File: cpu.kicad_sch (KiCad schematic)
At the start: 17 parts, among them IC1 68000CC

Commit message: Start PCB layout.
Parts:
- C15, C16, C17, C18, C2, C3, C5: footprint (none) -> Capacitor_SMD:C_0805_2012Metric
- IC1: value 68000CC -> 68HC000; footprint (none) -> Package_LCC:PLCC-68
- IC2: footprint (none) -> Package_SO:VSO-40_7.6x15.4mm_P0.762mm
- IC7: renamed from IC3; footprint (none) -> Package_SO:VSO-40_7.6x15.4mm_P0.762mm
- R3: footprint (none) -> Resistor_SMD:R_0805_2012Metric
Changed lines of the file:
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@@
       (effects (font (size 1.27 1.27)) (justify left))
     )
-    (property "Value" "68000CC" (at 171.1041 55.88 0)
-      (effects (font (size 1.27 1.27)) (justify left))
-    )
-    (property "Footprint" "" (at 166.37 115.57 0)
+    (property "Value" "68HC000" (at 171.1041 55.88 0)
+      (effects (font (size 1.27 1.27)) (justify left))
+    )
+    (property "Footprint" "Package_LCC:PLCC-68" (at 166.37 115.57 0)
       (effects (font (size 1.27 1.27)) hide)
     )
@@
       (effects (font (size 1.27 1.27)) (justify left))
     )
-    (property "Footprint" "" (at 66.3702 234.95 0)
+    (property "Footprint" "Capacitor_SMD:C_0805_2012Metric" (at 66.3702 234.95 0)
       (effects (font (size 1.27 1.27)) hide)
     )
@@
   (symbol (lib_id "MegaDrive:VRAM_64Kx8") (at 301.625 193.675 0) (unit 1)
     (in_bom yes) (on_board yes) (dnp no) (fields_autoplaced)
-    (property "Reference" "IC3" (at 305.0891 167.64 0)
+    (property "Reference" "IC7" (at 305.0891 167.64 0)
       (effects (font (size 1.27 1.27)) (justify left))
     )
@@
       (effects (font (size 1.27 1.27)))
     )
-    (property "Footprint" "" (at 302.26 196.85 0)
+    (property "Footprint" "Package_SO:VSO-40_7.6x15.4mm_P0.762mm" (at 302.26 196.85 0)
       (effects (font (size 1.27 1.27)) hide)
     )
@@
       (project "Neptune"
         (path "/bcc23b51-b742-4ae5-9dd6-d96a24058944/48e60f61-77cc-4ea0-898f-0029aa970ca5"
-          (reference "IC3") (unit 1)
+          (reference "IC7") (unit 1)
         )
       )
@@
       (effects (font (size 1.27 1.27)) (justify left))
     )
-    (property "Footprint" "" (at 350.8502 220.345 0)
+    (property "Footprint" "Capacitor_SMD:C_0805_2012Metric" (at 350.8502 220.345 0)
       (effects (font (size 1.27 1.27)) hide)
     )
@@
       (effects (font (size 1.27 1.27)) (justify right))
     )
-    (property "Footprint" "" (at 196.85 165.608 90)
+    (property "Footprint" "Resistor_SMD:R_0805_2012Metric" (at 196.85 165.608 90)
       (effects (font (size 1.27 1.27)) hide)
     )
@@
       (effects (font (size 1.27 1.27)) (justify left))
     )
-    (property "Footprint" "" (at 332.4098 220.345 0)
+    (property "Footprint" "Capacitor_SMD:C_0805_2012Metric" (at 332.4098 220.345 0)
       (effects (font (size 1.27 1.27)) hide)
     )
@@
       (effects (font (size 1.27 1.27)) (justify right))
     )
-    (property "Footprint" "" (at 135.255 137.668 90)
+    (property "Footprint" "Resistor_SMD:R_0805_2012Metric" (at 135.255 137.668 90)
       (effects (font (size 1.27 1.27)) hide)
     )
@@
       (effects (font (size 1.27 1.27)) (justify left))
     )
-    (property "Footprint" "" (at 359.1052 220.345 0)
+    (property "Footprint" "Capacitor_SMD:C_0805_2012Metric" (at 359.1052 220.345 0)
       (effects (font (size 1.27 1.27)) hide)
     )
@@
       (effects (font (size 1.27 1.27)) (justify left))
     )
-    (property "Footprint" "" (at 342.5952 220.345 0)
+    (property "Footprint" "Capacitor_SMD:C_0805_2012Metric" (at 342.5952 220.345 0)
       (effects (font (size 1.27 1.27)) hide)
     )
@@
       (effects (font (size 1.27 1.27)) (justify left))
     )
-    (property "Footprint" "" (at 272.1102 115.57 0)
+    (property "Footprint" "Capacitor_SMD:C_0805_2012Metric" (at 272.1102 115.57 0)
       (effects (font (size 1.27 1.27)) hide)
     )
@@
       (effects (font (size 1.27 1.27)) (justify left))
     )
-    (property "Footprint" "" (at 286.0802 115.57 0)
+    (property "Footprint" "Capacitor_SMD:C_0805_2012Metric" (at 286.0802 115.57 0)
       (effects (font (size 1.27 1.27)) hide)
     )
@@
       (effects (font (size 1.27 1.27)))
     )
-    (property "Footprint" "" (at 249.555 76.835 0)
+    (property "Footprint" "Package_SO:VSO-40_7.6x15.4mm_P0.762mm" (at 249.555 76.835 0)
       (effects (font (size 1.27 1.27)) hide)
     )
@@
         )
         (path "/bcc23b51-b742-4ae5-9dd6-d96a24058944/48e60f61-77cc-4ea0-898f-0029aa970ca5"
-          (reference "FB1") (unit 1)
-        )
-      )
+          (reference "FB7") (unit 1)
+        )
+      )

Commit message: Save first mock-up before updating footprints.
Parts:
- CA1, CA2, CA3, CA4: footprint (none) -> Resistor_SMD:R_Array_Convex_4x0603
- FB7: footprint (none) -> Inductor_SMD:L_0805_2012Metric
- IC2: footprint Package_SO:VSO-40_7.6x15.4mm_P0.762mm -> Neptune:SOIC-40
- IC7: footprint Package_SO:VSO-40_7.6x15.4mm_P0.762mm -> Neptune:SOJ-40
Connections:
- net SC renamed ~{SC}
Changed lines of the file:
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@@
     )
   )
-  (global_label "SC" (shape input) (at 365.76 209.55 0) (fields_autoplaced)
+  (global_label "~{SC}" (shape input) (at 365.76 209.55 0) (fields_autoplaced)
     (effects (font (size 1.27 1.27)) (justify left))
     (property "Intersheetrefs" "${INTERSHEET_REFS}" (at 371.2247 209.55 0)
@@
       (effects (font (size 1.27 1.27)) (justify left))
     )
-    (property "Footprint" "" (at 150.495 231.14 90)
+    (property "Footprint" "Resistor_SMD:R_Array_Convex_4x0603" (at 150.495 231.14 90)
       (effects (font (size 1.27 1.27)) hide)
     )
@@
       (effects (font (size 1.27 1.27)))
     )
-    (property "Footprint" "Package_SO:VSO-40_7.6x15.4mm_P0.762mm" (at 302.26 196.85 0)
+    (property "Footprint" "Neptune:SOJ-40" (at 302.26 196.85 0)
       (effects (font (size 1.27 1.27)) hide)
     )
@@
       (effects (font (size 1.27 1.27)) (justify left))
     )
-    (property "Footprint" "" (at 109.855 231.14 90)
+    (property "Footprint" "Resistor_SMD:R_Array_Convex_4x0603" (at 109.855 231.14 90)
       (effects (font (size 1.27 1.27)) hide)
     )
@@
       (effects (font (size 1.27 1.27)) (justify left))
     )
-    (property "Footprint" "" (at 130.175 231.14 90)
+    (property "Footprint" "Resistor_SMD:R_Array_Convex_4x0603" (at 130.175 231.14 90)
       (effects (font (size 1.27 1.27)) hide)
     )
@@
       (effects (font (size 1.27 1.27)) (justify left))
     )
-    (property "Footprint" "" (at 170.18 231.14 90)
+    (property "Footprint" "Resistor_SMD:R_Array_Convex_4x0603" (at 170.18 231.14 90)
       (effects (font (size 1.27 1.27)) hide)
     )
@@
       (effects (font (size 1.27 1.27)))
     )
-    (property "Footprint" "Package_SO:VSO-40_7.6x15.4mm_P0.762mm" (at 249.555 76.835 0)
+    (property "Footprint" "Neptune:SOIC-40" (at 249.555 76.835 0)
       (effects (font (size 1.27 1.27)) hide)
     )
@@
       (effects (font (size 1.27 1.27)))
     )
-    (property "Footprint" "" (at 135.255 61.468 90)
-      (effects (font (size 1.27 1.27)) hide)
-    )
+    (property "Footprint" "Inductor_SMD:L_0805_2012Metric" (at 135.255 61.468 90)
+      (effects (font (size 1.27 1.27)) hide)
+    )

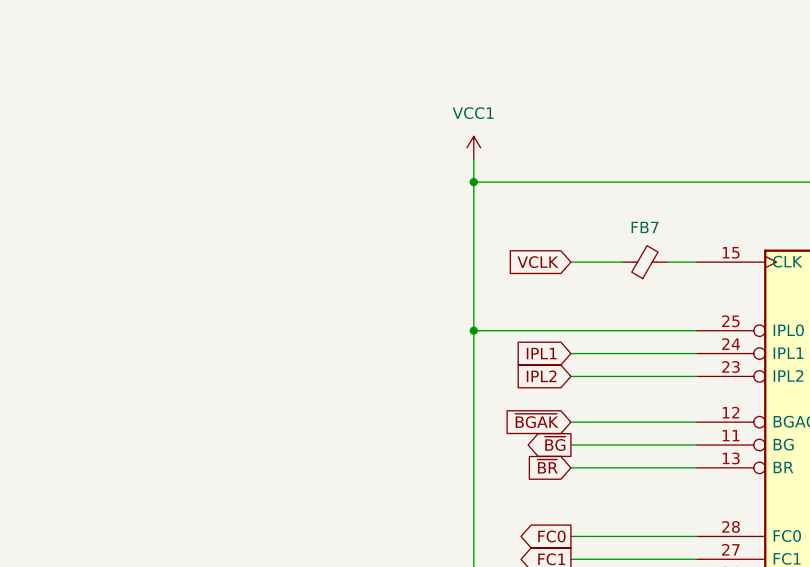
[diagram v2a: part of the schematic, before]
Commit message: Draft new layout with more accurate footprints.
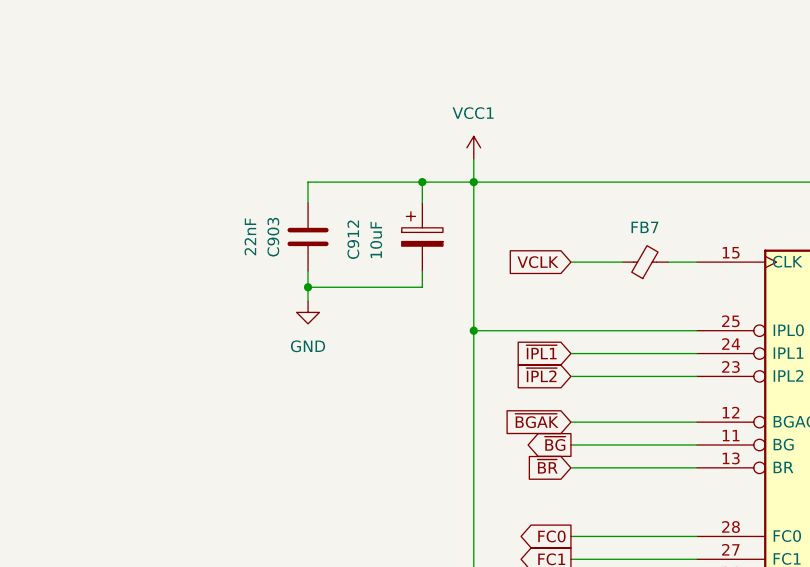
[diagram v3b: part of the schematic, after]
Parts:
- added C903: 22nF, Capacitor_SMD:C_0805_2012Metric, symbol Device:C
- added C912: 10uF, Capacitor_THT:CP_Radial_D5.0mm_P2.50mm, symbol Device:C_Polarized
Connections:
- net GND: now also C903.1, C912.2
- net VCC1: now also C903.2, C912.1
- net IPL1 renamed ~{IPL1}
- net IPL2 renamed ~{IPL2}
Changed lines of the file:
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@@
   (junction (at 118.11 241.3) (diameter 0) (color 0 0 0 0)
   )
+  (junction (at 97.79 62.484) (diameter 0) (color 0 0 0 0)
+  )
   (junction (at 158.115 241.3) (diameter 0) (color 0 0 0 0)
   )
@@
   )
   (junction (at 333.375 209.55) (diameter 0) (color 0 0 0 0)
+  )
+  (junction (at 110.49 50.8) (diameter 0) (color 0 0 0 0)
   )
   (junction (at 285.115 117.475) (diameter 0) (color 0 0 0 0)
@@
     (stroke (width 0) (type default))
   )
+  (wire (pts (xy 97.79 50.8) (xy 110.49 50.8))
+    (stroke (width 0) (type default))
+  )
   (bus (pts (xy 272.415 211.455) (xy 272.415 208.915))
     (stroke (width 0) (type default))
@@
     (stroke (width 0) (type default))
   )
+  (wire (pts (xy 97.79 53.086) (xy 97.79 50.8))
+    (stroke (width 0) (type default))
+  )
   (wire (pts (xy 349.885 220.345) (xy 349.885 222.885))
     (stroke (width 0) (type default))
@@
     (stroke (width 0) (type default))
   )
+  (wire (pts (xy 116.205 50.8) (xy 166.37 50.8))
+    (stroke (width 0) (type default))
+  )
   (bus (pts (xy 220.98 90.17) (xy 220.98 87.63))
     (stroke (width 0) (type default))
@@
     (stroke (width 0) (type default))
   )
+  (wire (pts (xy 110.49 50.8) (xy 116.205 50.8))
+    (stroke (width 0) (type default))
+  )
+  (wire (pts (xy 97.79 62.484) (xy 97.79 64.008))
+    (stroke (width 0) (type default))
+  )
   (wire (pts (xy 266.065 105.41) (xy 285.115 105.41))
     (stroke (width 0) (type default))
@@
     (stroke (width 0) (type default))
   )
+  (wire (pts (xy 110.49 62.484) (xy 97.79 62.484))
+    (stroke (width 0) (type default))
+  )
   (wire (pts (xy 285.115 117.475) (xy 271.145 117.475))
     (stroke (width 0) (type default))
@@
     (stroke (width 0) (type default))
   )
+  (wire (pts (xy 110.49 50.8) (xy 110.49 53.086))
+    (stroke (width 0) (type default))
+  )
   (wire (pts (xy 341.63 196.85) (xy 365.76 196.85))
     (stroke (width 0) (type default))
@@
     (stroke (width 0) (type default))
   )
+  (wire (pts (xy 97.79 60.706) (xy 97.79 62.484))
+    (stroke (width 0) (type default))
+  )
   (bus (pts (xy 277.495 92.71) (xy 277.495 90.17))
     (stroke (width 0) (type default))
@@
     (stroke (width 0) (type default))
   )
+  (wire (pts (xy 110.49 60.706) (xy 110.49 62.484))
+    (stroke (width 0) (type default))
+  )
   (bus (pts (xy 272.415 167.64) (xy 272.415 170.815))
     (stroke (width 0) (type default))
@@
   )
   (wire (pts (xy 191.77 110.49) (xy 200.66 110.49))
-    (stroke (width 0) (type default))
-  )
-  (wire (pts (xy 116.205 50.8) (xy 166.37 50.8))
     (stroke (width 0) (type default))
   )
@@
     )
   )
-  (global_label "IPL2" (shape input) (at 127 72.39 180) (fields_autoplaced)
+  (global_label "~{IPL2}" (shape input) (at 127 72.39 180) (fields_autoplaced)
     (effects (font (size 1.27 1.27)) (justify right))
     (property "Intersheetrefs" "${INTERSHEET_REFS}" (at 119.9024 72.39 0)
@@
     )
   )
-  (global_label "IPL1" (shape input) (at 127 69.85 180) (fields_autoplaced)
+  (global_label "~{IPL1}" (shape input) (at 127 69.85 180) (fields_autoplaced)
     (effects (font (size 1.27 1.27)) (justify right))
     (property "Intersheetrefs" "${INTERSHEET_REFS}" (at 119.9024 69.85 0)
@@
     )
   )
+  (symbol (lib_id "power:GND") (at 97.79 64.008 0) (mirror y) (unit 1)
+    (in_bom yes) (on_board yes) (dnp no) (fields_autoplaced)
+    (property "Reference" "#PWR010" (at 97.79 70.358 0)
+      (effects (font (size 1.27 1.27)) hide)
+    )
+    (property "Value" "GND" (at 97.79 69.088 0)
+      (effects (font (size 1.27 1.27)))
+    )
+    (property "Footprint" "" (at 97.79 64.008 0)
+      (effects (font (size 1.27 1.27)) hide)
+    )
+    (property "Datasheet" "" (at 97.79 64.008 0)
+      (effects (font (size 1.27 1.27)) hide)
+    )
+    (pin "1")
+    (instances
+      (project "PAC_SMAIN_RE"
+        (path "/0bedf059-ca5b-49fc-a202-5049da6fe5ec"
+          (reference "#PWR010") (unit 1)
+        )
+        (path "/0bedf059-ca5b-49fc-a202-5049da6fe5ec/e6e0d8a5-d653-452c-97ca-1b76da83b141"
+          (reference "#PWR09") (unit 1)
+        )
+      )
+      (project "Neptune"
+        (path "/bcc23b51-b742-4ae5-9dd6-d96a24058944/293c8f1f-2c58-4557-aeb8-8502bb66fbd4"
+          (reference "#PWR0154") (unit 1)
+        )
+        (path "/bcc23b51-b742-4ae5-9dd6-d96a24058944/48e60f61-77cc-4ea0-898f-0029aa970ca5"
+          (reference "#PWR0155") (unit 1)
+        )
+      )
+    )
+  )
   (symbol (lib_id "MegaDrive:C_Pack04") (at 102.87 231.14 0) (unit 1)
     (in_bom yes) (on_board yes) (dnp no)
@@
     )
   )
+  (symbol (lib_id "Device:C_Polarized") (at 110.49 56.896 0) (unit 1)
+    (in_bom yes) (on_board yes) (dnp no)
+    (property "Reference" "C912" (at 102.87 59.436 90)
+      (effects (font (size 1.27 1.27)) (justify left))
+    )
+    (property "Value" "10uF" (at 105.41 59.436 90)
+      (effects (font (size 1.27 1.27)) (justify left))
+    )
+    (property "Footprint" "Capacitor_THT:CP_Radial_D5.0mm_P2.50mm" (at 111.4552 60.706 0)
+      (effects (font (size 1.27 1.27)) hide)
+    )
+    (property "Datasheet" "~" (at 110.49 56.896 0)
+      (effects (font (size 1.27 1.27)) hide)
+    )
+    (pin "1")
+    (pin "2")
+    (instances
+      (project "Neptune"
+        (path "/bcc23b51-b742-4ae5-9dd6-d96a24058944/01513199-62c5-4123-a151-ccd381a5e6c1"
+          (reference "C912") (unit 1)
+        )
+        (path "/bcc23b51-b742-4ae5-9dd6-d96a24058944/293c8f1f-2c58-4557-aeb8-8502bb66fbd4"
+          (reference "CE21") (unit 1)
+        )
+        (path "/bcc23b51-b742-4ae5-9dd6-d96a24058944/48e60f61-77cc-4ea0-898f-0029aa970ca5"
+          (reference "CE20") (unit 1)
+        )
+      )
+    )
+  )
   (symbol (lib_id "power:GND") (at 165.735 243.84 0) (unit 1)
     (in_bom yes) (on_board yes) (dnp no) (fields_autoplaced)
@@
         )
       )
+    )
+  )
+  (symbol (lib_id "Device:C") (at 97.79 56.896 180) (unit 1)
+    (in_bom yes) (on_board yes) (dnp no)
+    (property "Reference" "C903" (at 93.98 56.896 90)
+      (effects (font (size 1.27 1.27)))
+    )
+    (property "Value" "22nF" (at 91.44 56.896 90)
+      (effects (font (size 1.27 1.27)))
+    )
+    (property "Footprint" "Capacitor_SMD:C_0805_2012Metric" (at 96.8248 53.086 0)
+      (effects (font (size 1.27 1.27)) hide)
+    )
+    (property "Datasheet" "~" (at 97.79 56.896 0)
+      (effects (font (size 1.27 1.27)) hide)
+    )
+    (pin "1")
+    (pin "2")
+    (instances
+      (project "Neptune"
+        (path "/bcc23b51-b742-4ae5-9dd6-d96a24058944/01513199-62c5-4123-a151-ccd381a5e6c1"
+          (reference "C903") (unit 1)
+        )
+        (path "/bcc23b51-b742-4ae5-9dd6-d96a24058944/293c8f1f-2c58-4557-aeb8-8502bb66fbd4"
+          (reference "C41") (unit 1)
+        )
+        (path "/bcc23b51-b742-4ae5-9dd6-d96a24058944/48e60f61-77cc-4ea0-898f-0029aa970ca5"
+          (reference "C37") (unit 1)
+        )
+      )

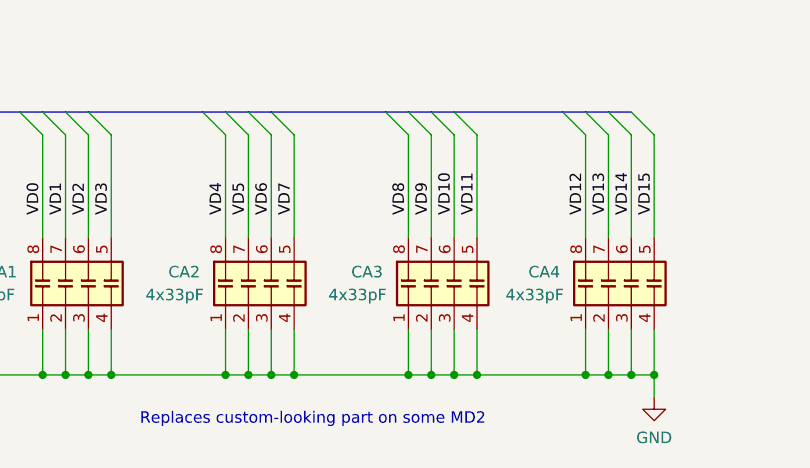
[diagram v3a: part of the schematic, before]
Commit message: Place remaining passives.
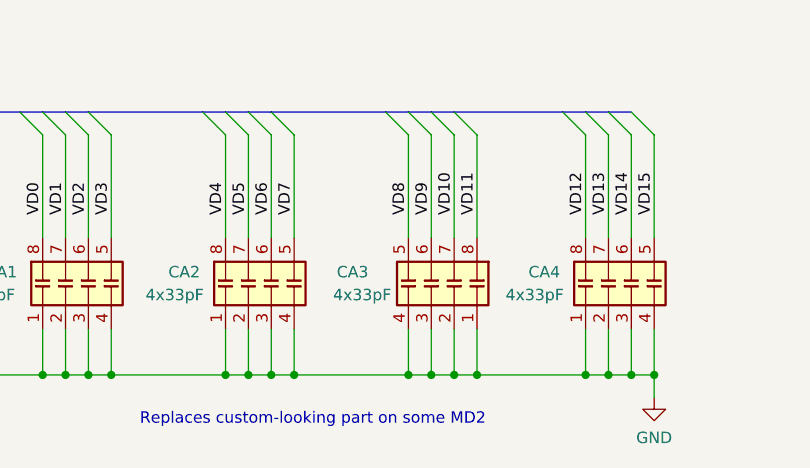
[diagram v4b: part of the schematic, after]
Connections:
- net VD10: now also CA3.7 (R2.2); no longer CA3.6 (R3.2)
- net VD11: now also CA3.8 (R1.2); no longer CA3.5 (R4.2)
- net VD8: now also CA3.5 (R4.2); no longer CA3.8 (R1.2)
- net VD9: now also CA3.6 (R3.2); no longer CA3.7 (R2.2)
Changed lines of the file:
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@@
     )
   )
-  (symbol (lib_id "MegaDrive:C_Pack04") (at 143.51 231.14 0) (unit 1)
+  (symbol (lib_id "MegaDrive:C_Pack04") (at 140.97 231.14 0) (mirror y) (unit 1)
     (in_bom yes) (on_board yes) (dnp no)
-    (property "Reference" "CA3" (at 132.08 229.87 0)
+    (property "Reference" "CA3" (at 133.985 229.87 0)
       (effects (font (size 1.27 1.27)) (justify left))
     )
-    (property "Value" "4x33pF" (at 129.54 232.41 0)
+    (property "Value" "4x33pF" (at 136.525 232.41 0)
       (effects (font (size 1.27 1.27)) (justify left))
     )
-    (property "Footprint" "Resistor_SMD:R_Array_Convex_4x0603" (at 150.495 231.14 90)
+    (property "Footprint" "Resistor_SMD:R_Array_Convex_4x0603" (at 133.985 231.14 90)
       (effects (font (size 1.27 1.27)) hide)
     )

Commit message: Some power routing.
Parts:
- added C903 (x2): 22nF, Capacitor_SMD:C_0805_2012Metric, symbol Device:C
- added C912: 10uF, Capacitor_THT:CP_Radial_D5.0mm_P2.50mm, symbol Device:C_Polarized
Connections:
- net GND: now also C903.1, C903.1, C912.2
- net VCC1: now also C903.2, C903.2, C912.1
